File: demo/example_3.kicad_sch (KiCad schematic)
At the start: 6 parts, among them U2 MIC841HYC5

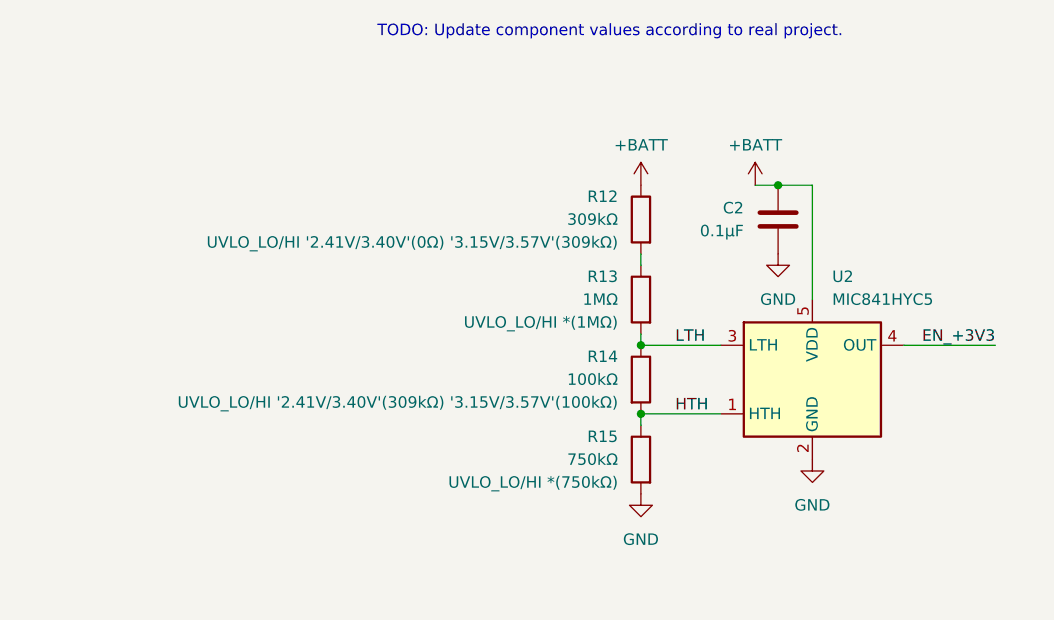
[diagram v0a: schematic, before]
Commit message: Update demo project for upcoming changes
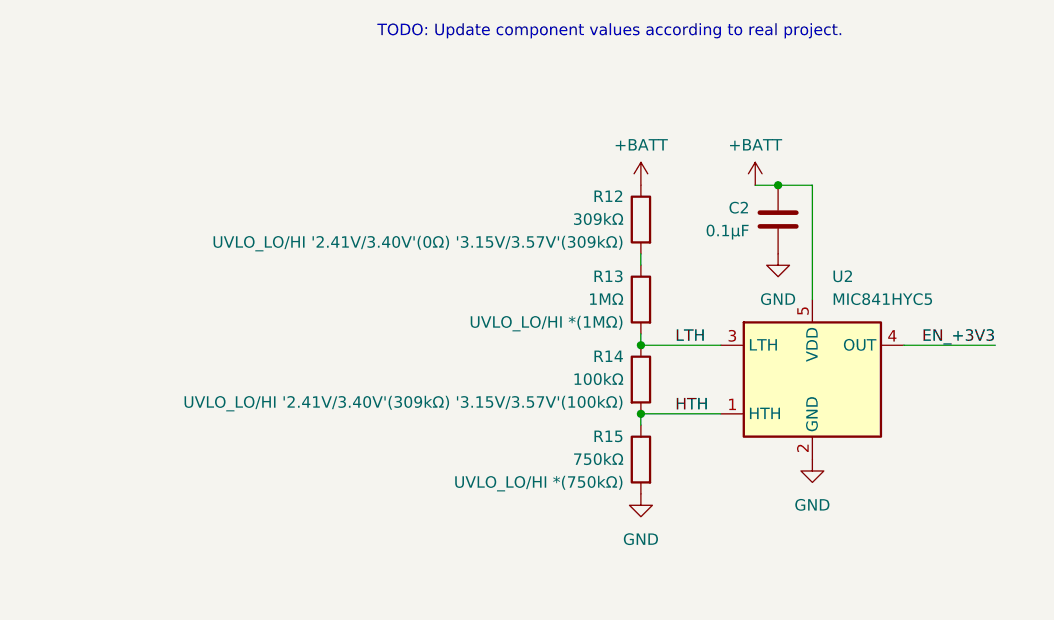
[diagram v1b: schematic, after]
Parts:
- R12: KiVar.Rule UVLO_LO/HI '2.41V/3.40V'(0Ω) '3.15V/3.57V'(309kΩ) -> (none); Var (none) -> UVLO_LO/HI '2.41V/3.40V'(0Ω) '3.15V/3.57V'(309kΩ)
- R13: KiVar.Rule UVLO_LO/HI *(1MΩ) -> (none); Var (none) -> UVLO_LO/HI *(1MΩ)
- R14: KiVar.Rule UVLO_LO/HI '2.41V/3.40V'(309kΩ) '3.15V/3.57V'(100kΩ) -> (none); Var (none) -> UVLO_LO/HI '2.41V/3.40V'(309kΩ) '3.15V/3.57V'(100kΩ)
- R15: KiVar.Rule UVLO_LO/HI *(750kΩ) -> (none); Var (none) -> UVLO_LO/HI *(750kΩ)
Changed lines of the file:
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@@
 	(title_block
 		(title "KiVar Demo")
-		(date "2024-03-18")
+		(date "2024-03-19")
 		(company "Author: Mark Hämmerling <dev@markh.de>")
 		(comment 1 "https://github.com/markh-de/KiVar")
@@
 		(on_board yes)
 		(dnp no)
+		(fields_autoplaced yes)
 		(property "Reference" "R14"
-			(at 106.045 66.0399 0)
+			(at 106.68 66.0399 0)
 			(effects
 				(font
@@
 		)
 		(property "Value" "100kΩ"
-			(at 106.045 68.5799 0)
+			(at 106.68 68.5799 0)
 			(effects
 				(font
@@
 			)
 		)
-		(property "KiVar.Rule" "UVLO_LO/HI '2.41V/3.40V'(309kΩ) '3.15V/3.57V'(100kΩ)"
-			(at 106.045 71.1199 0)
+		(property "Var" "UVLO_LO/HI '2.41V/3.40V'(309kΩ) '3.15V/3.57V'(100kΩ)"
+			(at 106.68 71.1199 0)
 			(effects
 				(font
@@
 		(on_board yes)
 		(dnp no)
+		(fields_autoplaced yes)
 		(property "Reference" "R12"
-			(at 106.045 48.2599 0)
+			(at 106.68 48.2599 0)
 			(effects
 				(font
@@
 		)
 		(property "Value" "309kΩ"
-			(at 106.045 50.7999 0)
+			(at 106.68 50.7999 0)
 			(effects
 				(font
@@
 			)
 		)
-		(property "KiVar.Rule" "UVLO_LO/HI '2.41V/3.40V'(0Ω) '3.15V/3.57V'(309kΩ)"
-			(at 106.045 53.3399 0)
+		(property "Var" "UVLO_LO/HI '2.41V/3.40V'(0Ω) '3.15V/3.57V'(309kΩ)"
+			(at 106.68 53.3399 0)
 			(effects
 				(font
@@
 		(fields_autoplaced yes)
 		(property "Reference" "C2"
-			(at 120.015 49.5299 0)
+			(at 120.65 49.5299 0)
 			(effects
 				(font
@@
 		)
 		(property "Value" "0.1µF"
-			(at 120.015 52.0699 0)
+			(at 120.65 52.0699 0)
 			(effects
 				(font
@@
 		(on_board yes)
 		(dnp no)
+		(fields_autoplaced yes)
 		(property "Reference" "R15"
-			(at 106.045 74.9299 0)
+			(at 106.68 74.9299 0)
 			(effects
 				(font
@@
 		)
 		(property "Value" "750kΩ"
-			(at 106.045 77.4699 0)
+			(at 106.68 77.4699 0)
 			(effects
 				(font
@@
 			)
 		)
-		(property "KiVar.Rule" "UVLO_LO/HI *(750kΩ)"
-			(at 106.045 80.0099 0)
+		(property "Var" "UVLO_LO/HI *(750kΩ)"
+			(at 106.68 80.0099 0)
 			(effects
 				(font
@@
 		(on_board yes)
 		(dnp no)
+		(fields_autoplaced yes)
 		(property "Reference" "R13"
-			(at 106.045 57.1499 0)
+			(at 106.68 57.1499 0)
 			(effects
 				(font
@@
 		)
 		(property "Value" "1MΩ"
-			(at 106.045 59.6899 0)
+			(at 106.68 59.6899 0)
 			(effects
 				(font
@@
 			)
 		)
-		(property "KiVar.Rule" "UVLO_LO/HI *(1MΩ)"
-			(at 106.045 62.2299 0)
-			(effects
-				(font
+		(property "Var" "UVLO_LO/HI *(1MΩ)"
+			(at 106.68 62.2299 0)
+			(effects
+				(font

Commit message: Make use of new 0.2.0 features in demo project, use different expression types
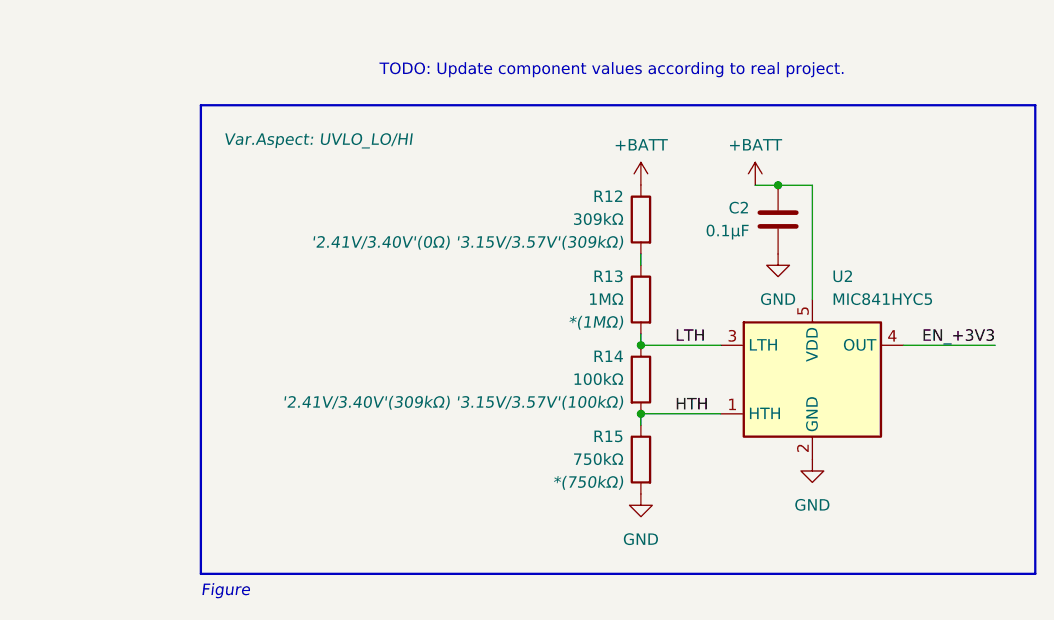
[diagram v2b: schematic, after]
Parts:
- R12: Var UVLO_LO/HI '2.41V/3.40V'(0Ω) '3.15V/3.57V'(309kΩ) -> '2.41V/3.40V'(0Ω) '3.15V/3.57V'(309kΩ); Var.Aspect (none) -> UVLO_LO/HI
- R13: Var UVLO_LO/HI *(1MΩ) -> *(1MΩ); Var.Aspect (none) -> UVLO_LO/HI
- R14: Var UVLO_LO/HI '2.41V/3.40V'(309kΩ) '3.15V/3.57V'(100kΩ) -> '2.41V/3.40V'(309kΩ) '3.15V/3.57V'(100kΩ); Var.Aspect (none) -> UVLO_LO/HI
- R15: Var UVLO_LO/HI *(750kΩ) -> *(750kΩ); Var.Aspect (none) -> UVLO_LO/HI
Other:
- note added: "Figure"
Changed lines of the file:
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@@
+		)
+	)
+	(rectangle
+		(start 59.69 38.1)
+		(end 152.4 90.17)
+		(stroke
+			(width 0.254)
+			(type default)
+			(color 72 72 72 1)
+		)
+		(fill
+			(type none)
 		)
 	)
 	(text "TODO: Update component values according to real project."
 		(exclude_from_sim no)
-		(at 105.156 29.972 0)
+		(at 105.41 34.29 0)
 		(effects
 			(font
@@
 		)
 	)
-	(label "EN_+3V3"
-		(at 147.955 64.77 180)
-		(fields_autoplaced yes)
+	(text "Figure"
+		(exclude_from_sim no)
+		(at 59.69 91.44 0)
 		(effects
 			(font
 				(size 1.27 1.27)
-			)
-			(justify right bottom)
-		)
-	)
-	(label "LTH"
-		(at 112.395 64.77 0)
+				(italic yes)
+				(color 72 72 72 1)
+			)
+			(justify left top)
+		)
+	)
+	(label "EN_+3V3"
+		(at 147.955 64.77 180)
 		(fields_autoplaced yes)
 		(effects
@@
 				(size 1.27 1.27)
 			)
-			(justify left bottom)
-		)
-	)
-	(label "HTH"
-		(at 112.395 72.39 0)
+			(justify right bottom)
+		)
+	)
+	(label "LTH"
+		(at 112.395 64.77 0)
 		(fields_autoplaced yes)
 		(effects
@@
 		)
 	)
+	(label "HTH"
+		(at 112.395 72.39 0)
+		(fields_autoplaced yes)
+		(effects
+			(font
+				(size 1.27 1.27)
+			)
+			(justify left bottom)
+		)
+	)
 	(symbol
 		(lib_id "power:GND")
@@
 			)
 		)
-		(property "Var" "UVLO_LO/HI '2.41V/3.40V'(309kΩ) '3.15V/3.57V'(100kΩ)"
+		(property "Var" "'2.41V/3.40V'(309kΩ) '3.15V/3.57V'(100kΩ)"
 			(at 106.68 71.1199 0)
 			(effects
 				(font
 					(size 1.27 1.27)
+					(italic yes)
 				)
 				(justify right)
+			)
+		)
+		(property "Var.Aspect" "UVLO_LO/HI"
+			(at 108.585 68.58 0)
+			(effects
+				(font
+					(size 1.27 1.27)
+				)
+				(hide yes)
 			)
 		)
@@
 		(on_board yes)
 		(dnp no)
-		(fields_autoplaced yes)
 		(property "Reference" "R12"
 			(at 106.68 48.2599 0)
@@
 			)
 		)
-		(property "Var" "UVLO_LO/HI '2.41V/3.40V'(0Ω) '3.15V/3.57V'(309kΩ)"
+		(property "Var" "'2.41V/3.40V'(0Ω) '3.15V/3.57V'(309kΩ)"
 			(at 106.68 53.3399 0)
 			(effects
 				(font
 					(size 1.27 1.27)
-				)
-				(justify left)
+					(italic yes)
+				)
+				(justify left)
+			)
+		)
+		(property "Var.Aspect" "UVLO_LO/HI"
+			(at 62.23 41.91 0)
+			(show_name yes)
+			(do_not_autoplace yes)
+			(effects
+				(font
+					(size 1.27 1.27)
+					(italic yes)
+				)
+				(justify right)
 			)
 		)
@@
 			)
 		)
-		(property "Var" "UVLO_LO/HI *(750kΩ)"
+		(property "Var" "*(750kΩ)"
 			(at 106.68 80.0099 0)
 			(effects
 				(font
 					(size 1.27 1.27)
-				)
-				(justify left)
+					(italic yes)
+				)
+				(justify left)
+			)
+		)
+		(property "Var.Aspect" "UVLO_LO/HI"
+			(at 108.585 77.47 0)
+			(effects
+				(font
+					(size 1.27 1.27)
+				)
+				(hide yes)
 			)
 		)
@@
 			)
 		)
-		(property "Var" "UVLO_LO/HI *(1MΩ)"
+		(property "Var" "*(1MΩ)"
 			(at 106.68 62.2299 0)
 			(effects
 				(font
 					(size 1.27 1.27)
-				)
-				(justify left)
-			)
-		)
+					(italic yes)
+				)
+				(justify left)
+			)
+		)
+		(property "Var.Aspect" "UVLO_LO/HI"
+			(at 108.585 59.69 0)
+			(effects
+				(font
+					(size 1.27 1.27)
+				)
+				(hide yes)
+			)
+		)
